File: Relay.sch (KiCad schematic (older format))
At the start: 11 parts, among them K1 1461069-5, Q1 2N3904, U1 LTV-816S

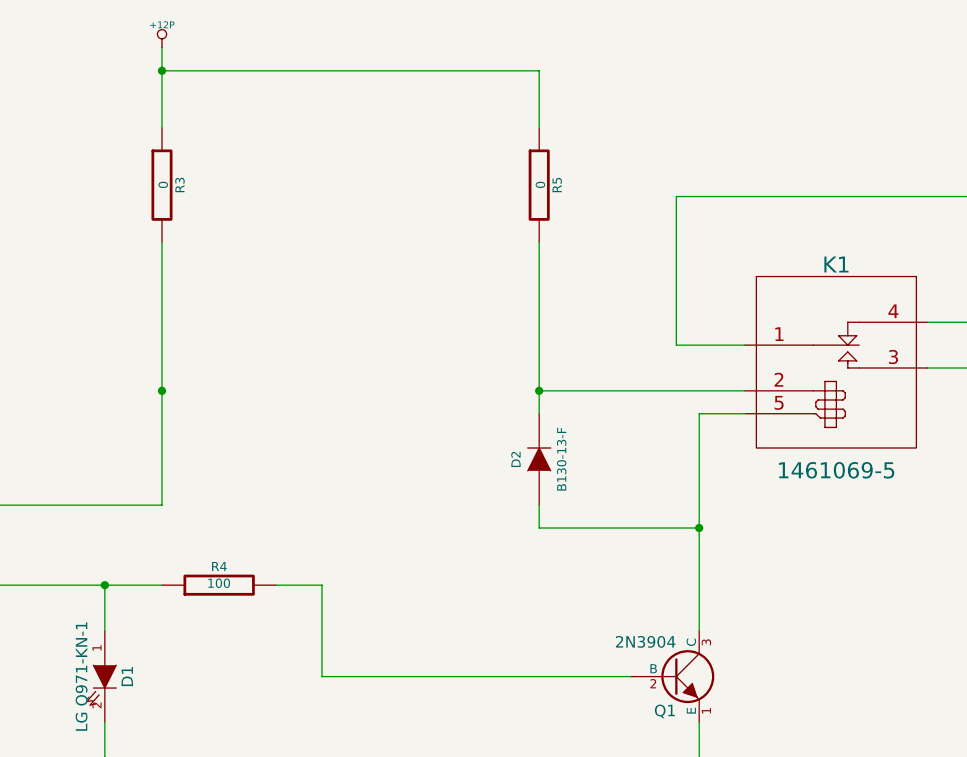
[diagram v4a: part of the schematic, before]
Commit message: Layout Work Session 18 Output
Added test points, changed a bunch of silk screen, added another
mounting hole and added a placeholder for the final commit number of the
board being sent to fab.
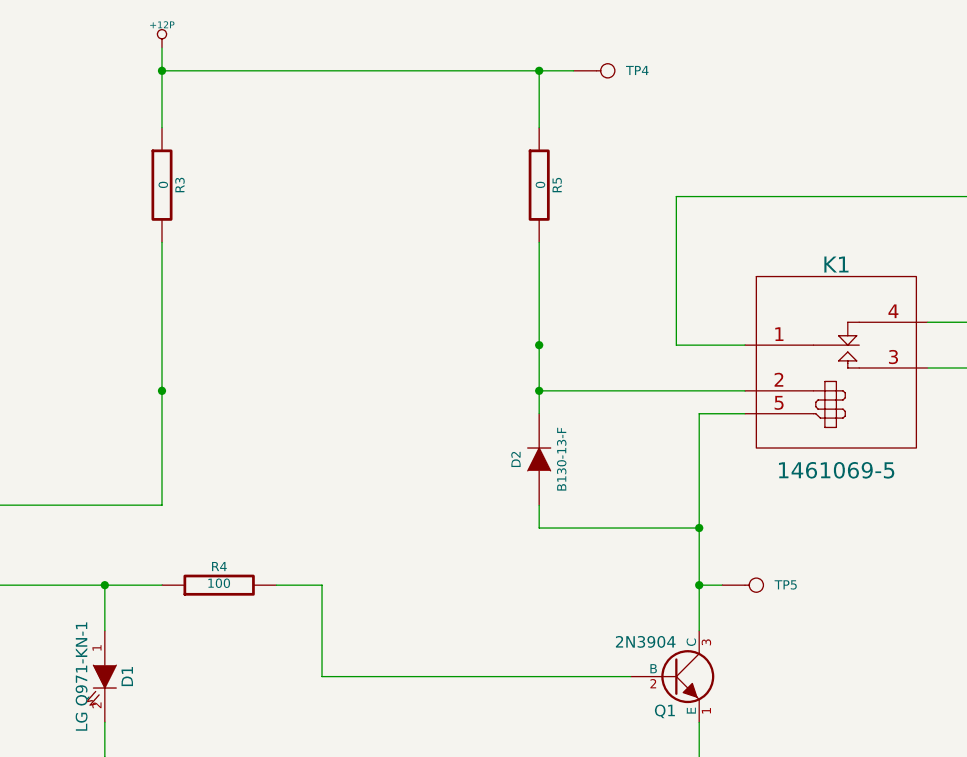
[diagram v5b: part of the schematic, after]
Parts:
- added TP4: +12P, symbol CONN_1
- added TP5: RELAY_LOW, symbol CONN_1
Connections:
- net +12P: now also TP4.1
- net at D2.1 (A), K1.5 (COIL-), Q1.3 (C): now also TP5.1
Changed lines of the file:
@@
-EESchema Schematic File Version 2  date 12/3/2013 1:00:45 AM
+EESchema Schematic File Version 2  date 12/18/2013 11:27:15 PM
 LIBS:power
 LIBS:device
@@
 Sheet 4 9
 Title ""
-Date "3 dec 2013"
+Date "19 dec 2013"
 Rev ""
 Comp ""
@@
 	8100 1800 8100 1550
 Wire Wire Line
-	8100 1550 6450 1550
+	6450 1550 8250 1550
 Connection ~ 6450 1550
 $Comp
@@
 	1    0    0    -1
 $EndComp
+$Comp
+L CONN_1 TP5
+U 1 1 52B28C6E
+P 9050 3800
+F 0 "TP5" H 9130 3800 40  0000 L CNN
+F 1 "RELAY_LOW" H 9050 3855 30  0001 C CNN
+F 2 "" H 9050 3800 60  0000 C CNN
+F 3 "" H 9050 3800 60  0000 C CNN
+	1    9050 3800
+	1    0    0    -1
+$EndComp
+Connection ~ 8100 2750
+Wire Wire Line
+	8900 3800 8800 3800
+Connection ~ 8800 3800
+$Comp
+L CONN_1 TP4
+U 1 1 52B28CD2
+P 8400 1550
+F 0 "TP4" H 8480 1550 40  0000 L CNN
+F 1 "+12P" H 8400 1605 30  0001 C CNN
+F 2 "" H 8400 1550 60  0000 C CNN
+F 3 "" H 8400 1550 60  0000 C CNN
+	1    8400 1550
+	1    0    0    -1
+$EndComp
+Connection ~ 8100 1550
 $EndSCHEMATC

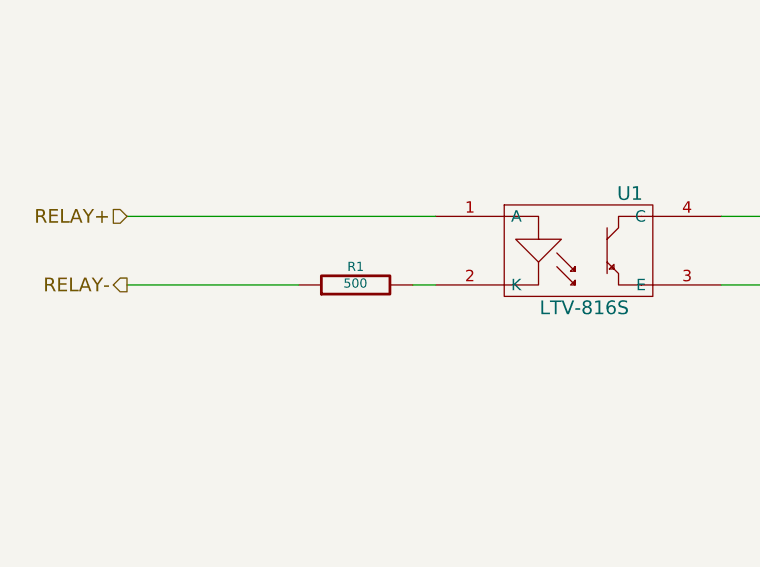
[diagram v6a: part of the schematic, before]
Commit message: Added Passive Values and SPICE models
As part of week 1 of Session 1B, we added a SPICE model of the In amp
and went through and assigned values to all of the passive components.
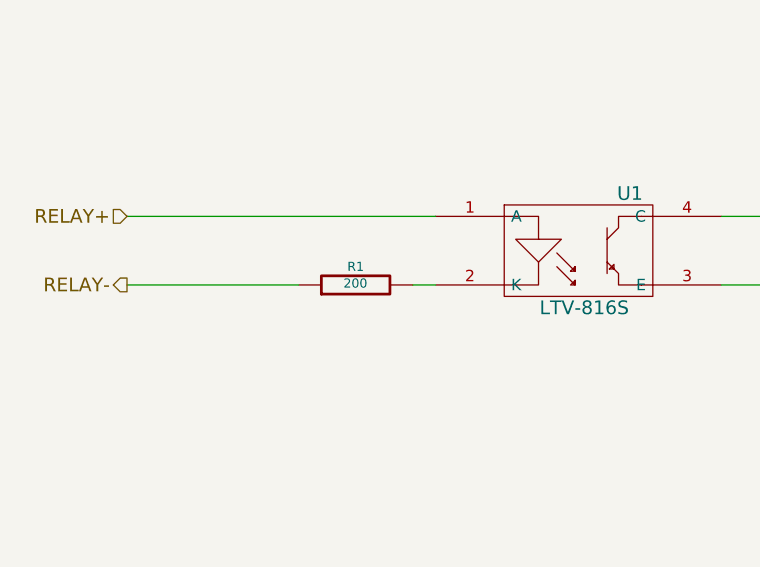
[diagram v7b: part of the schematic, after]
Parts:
- R1: value 500 -> 200
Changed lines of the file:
@@
-EESchema Schematic File Version 2  date 2/16/2014 3:41:32 PM
+EESchema Schematic File Version 2  date 4/16/2014 11:04:06 PM
 LIBS:power
 LIBS:device
@@
 Sheet 4 9
 Title ""
-Date "16 feb 2014"
+Date "17 apr 2014"
 Rev ""
 Comp ""
@@
 P 3300 3750
 F 0 "R1" V 3380 3750 40  0000 C CNN
-F 1 "500" V 3307 3751 40  0000 C CNN
+F 1 "200" V 3307 3751 40  0000 C CNN
 F 2 "~" V 3230 3750 30  0000 C CNN
 F 3 "~" H 3300 3750 30  0000 C CNN

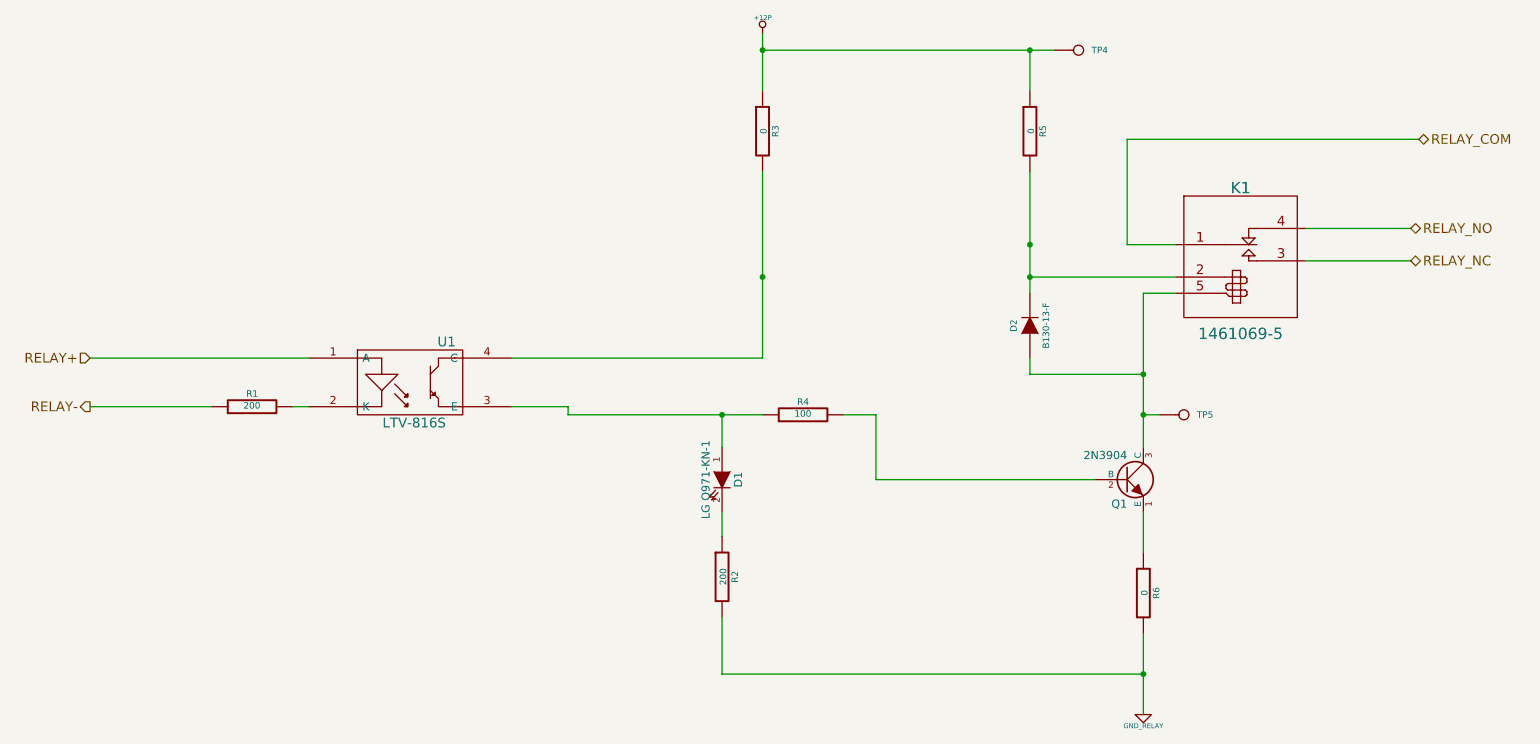
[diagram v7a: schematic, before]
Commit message: Added the schematic and BOM changes back in after hard reset
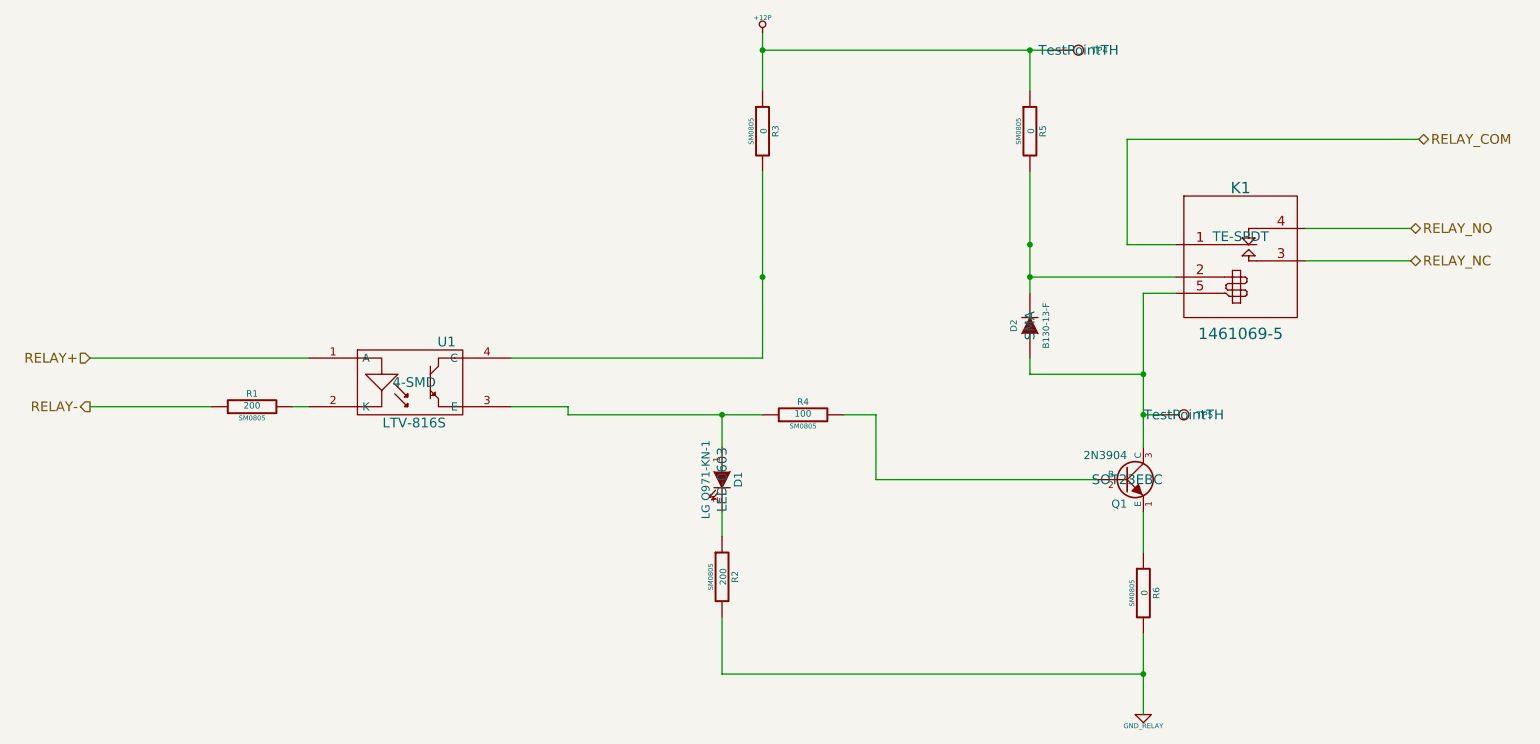
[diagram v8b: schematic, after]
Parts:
- D1: footprint ~ -> LED-0603
- D2: footprint ~ -> SMA
- K1: footprint ~ -> TE-SPDT
- Q1: footprint ~ -> SOT23EBC
- R1, R2, R3, R4, R5, R6: footprint ~ -> SM0805
- TP4, TP5: footprint (none) -> TestPointTH
- U1: footprint (none) -> 4-SMD
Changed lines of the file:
@@
-EESchema Schematic File Version 2  date 4/16/2014 11:04:06 PM
+EESchema Schematic File Version 2  date 4/18/2014 9:49:53 PM
 LIBS:power
 LIBS:device
@@
 Sheet 4 9
 Title ""
-Date "17 apr 2014"
+Date "19 apr 2014"
 Rev ""
 Comp ""
@@
 F 0 "R4" V 6780 3800 40  0000 C CNN
 F 1 "100" V 6707 3801 40  0000 C CNN
-F 2 "~" V 6630 3800 30  0000 C CNN
+F 2 "SM0805" V 6630 3800 30  0000 C CNN
 F 3 "~" H 6700 3800 30  0000 C CNN
 	1    6700 3800
@@
 F 0 "Q1" H 8700 4050 50  0000 R CNN
 F 1 "2N3904" H 8700 4350 50  0000 R CNN
-F 2 "~" H 8700 4200 60  0000 C CNN
+F 2 "SOT23EBC" H 8700 4200 60  0000 C CNN
 F 3 "~" H 8700 4200 60  0000 C CNN
 F 4 "Diodes Inc" H 8700 4200 60  0001 C CNN "MFG Name"
@@
 F 0 "D1" H 6200 4300 50  0000 C CNN
 F 1 "LG Q971-KN-1" H 6200 4100 50  0000 C CNN
-F 2 "~" H 6200 4200 60  0000 C CNN
+F 2 "LED-0603" H 6200 4200 60  0000 C CNN
 F 3 "~" H 6200 4200 60  0000 C CNN
 	1    6200 4200
@@
 F 0 "K1" H 9400 3000 70  0000 C CNN
 F 1 "1461069-5" H 9400 2100 70  0000 C CNN
-F 2 "~" H 9400 2700 60  0000 C CNN
+F 2 "TE-SPDT" H 9400 2700 60  0000 C CNN
 F 3 "~" H 9400 2700 60  0000 C CNN
 	1    9400 2700
@@
 F 0 "R6" V 8880 4900 40  0000 C CNN
 F 1 "0" V 8807 4901 40  0000 C CNN
-F 2 "~" V 8730 4900 30  0000 C CNN
+F 2 "SM0805" V 8730 4900 30  0000 C CNN
 F 3 "~" H 8800 4900 30  0000 C CNN
 	1    8800 4900
@@
 F 0 "R2" V 6280 4800 40  0000 C CNN
 F 1 "200" V 6207 4801 40  0000 C CNN
-F 2 "~" V 6130 4800 30  0000 C CNN
+F 2 "SM0805" V 6130 4800 30  0000 C CNN
 F 3 "~" H 6200 4800 30  0000 C CNN
 	1    6200 4800
@@
 F 0 "R3" V 6530 2050 40  0000 C CNN
 F 1 "0" V 6457 2051 40  0000 C CNN
-F 2 "~" V 6380 2050 30  0000 C CNN
+F 2 "SM0805" V 6380 2050 30  0000 C CNN
 F 3 "~" H 6450 2050 30  0000 C CNN
 	1    6450 2050
@@
 F 0 "R1" V 3380 3750 40  0000 C CNN
 F 1 "200" V 3307 3751 40  0000 C CNN
-F 2 "~" V 3230 3750 30  0000 C CNN
+F 2 "SM0805" V 3230 3750 30  0000 C CNN
 F 3 "~" H 3300 3750 30  0000 C CNN
 	1    3300 3750
@@
 F 0 "U1" H 4500 3850 60  0000 C CNN
 F 1 "LTV-816S" H 4300 3350 60  0000 C CNN
-F 2 "" H 4300 3600 60  0000 C CNN
+F 2 "4-SMD" H 4300 3600 60  0000 C CNN
 F 3 "" H 4300 3600 60  0000 C CNN
 F 4 "LTV-816S" H 4300 3600 60  0001 C CNN "MFG Part Number"
@@
 F 0 "D2" H 8100 3350 40  0000 C CNN
 F 1 "B130-13-F" H 8100 3150 40  0000 C CNN
-F 2 "~" H 8100 3250 60  0000 C CNN
+F 2 "SMA" H 8100 3250 60  0000 C CNN
 F 3 "~" H 8100 3250 60  0000 C CNN
 	1    8100 3250
@@
 F 0 "R5" V 8180 2050 40  0000 C CNN
 F 1 "0" V 8107 2051 40  0000 C CNN
-F 2 "~" V 8030 2050 30  0000 C CNN
+F 2 "SM0805" V 8030 2050 30  0000 C CNN
 F 3 "~" H 8100 2050 30  0000 C CNN
 	1    8100 2050
@@
 F 0 "TP5" H 9130 3800 40  0000 L CNN
 F 1 "RELAY_LOW" H 9050 3855 30  0001 C CNN
-F 2 "" H 9050 3800 60  0000 C CNN
+F 2 "TestPointTH" H 9050 3800 60  0000 C CNN
 F 3 "" H 9050 3800 60  0000 C CNN
 	1    9050 3800
@@
 F 0 "TP4" H 8480 1550 40  0000 L CNN
 F 1 "+12P" H 8400 1605 30  0001 C CNN
-F 2 "" H 8400 1550 60  0000 C CNN
+F 2 "TestPointTH" H 8400 1550 60  0000 C CNN
 F 3 "" H 8400 1550 60  0000 C CNN
 	1    8400 1550
